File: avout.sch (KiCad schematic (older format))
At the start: 47 parts, among them CN6 AUDIO_VIDEO, M1 Modulator, Q3 2SC1815, Q81 BC547, Q82 BC547

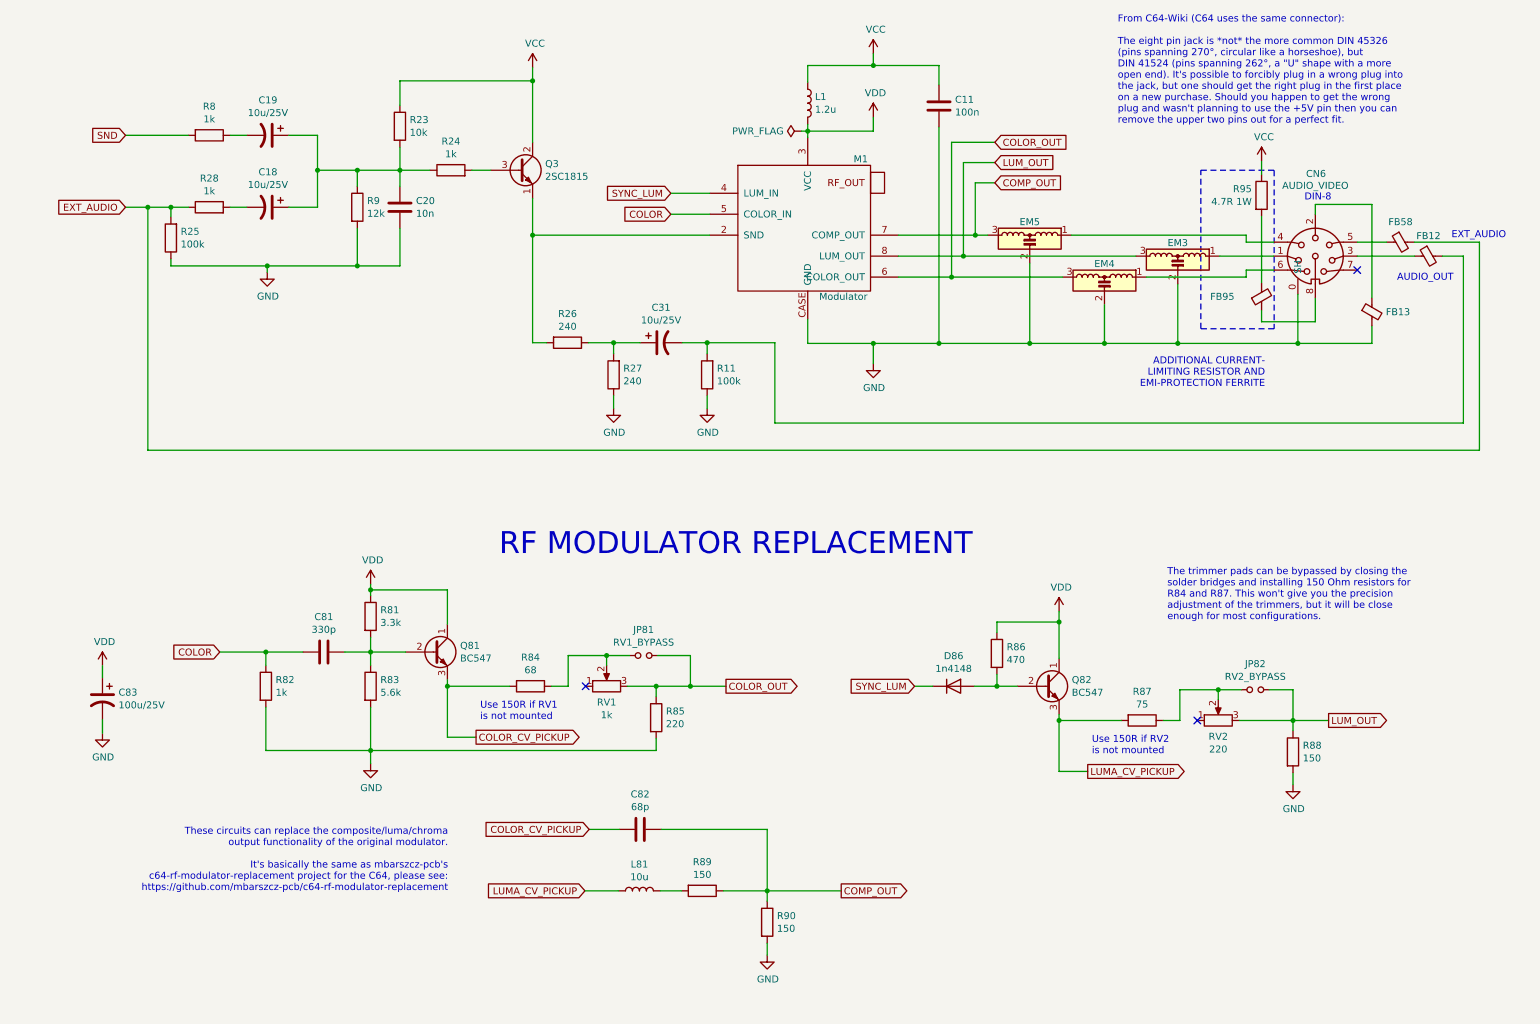
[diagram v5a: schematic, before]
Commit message: Isolate video ground
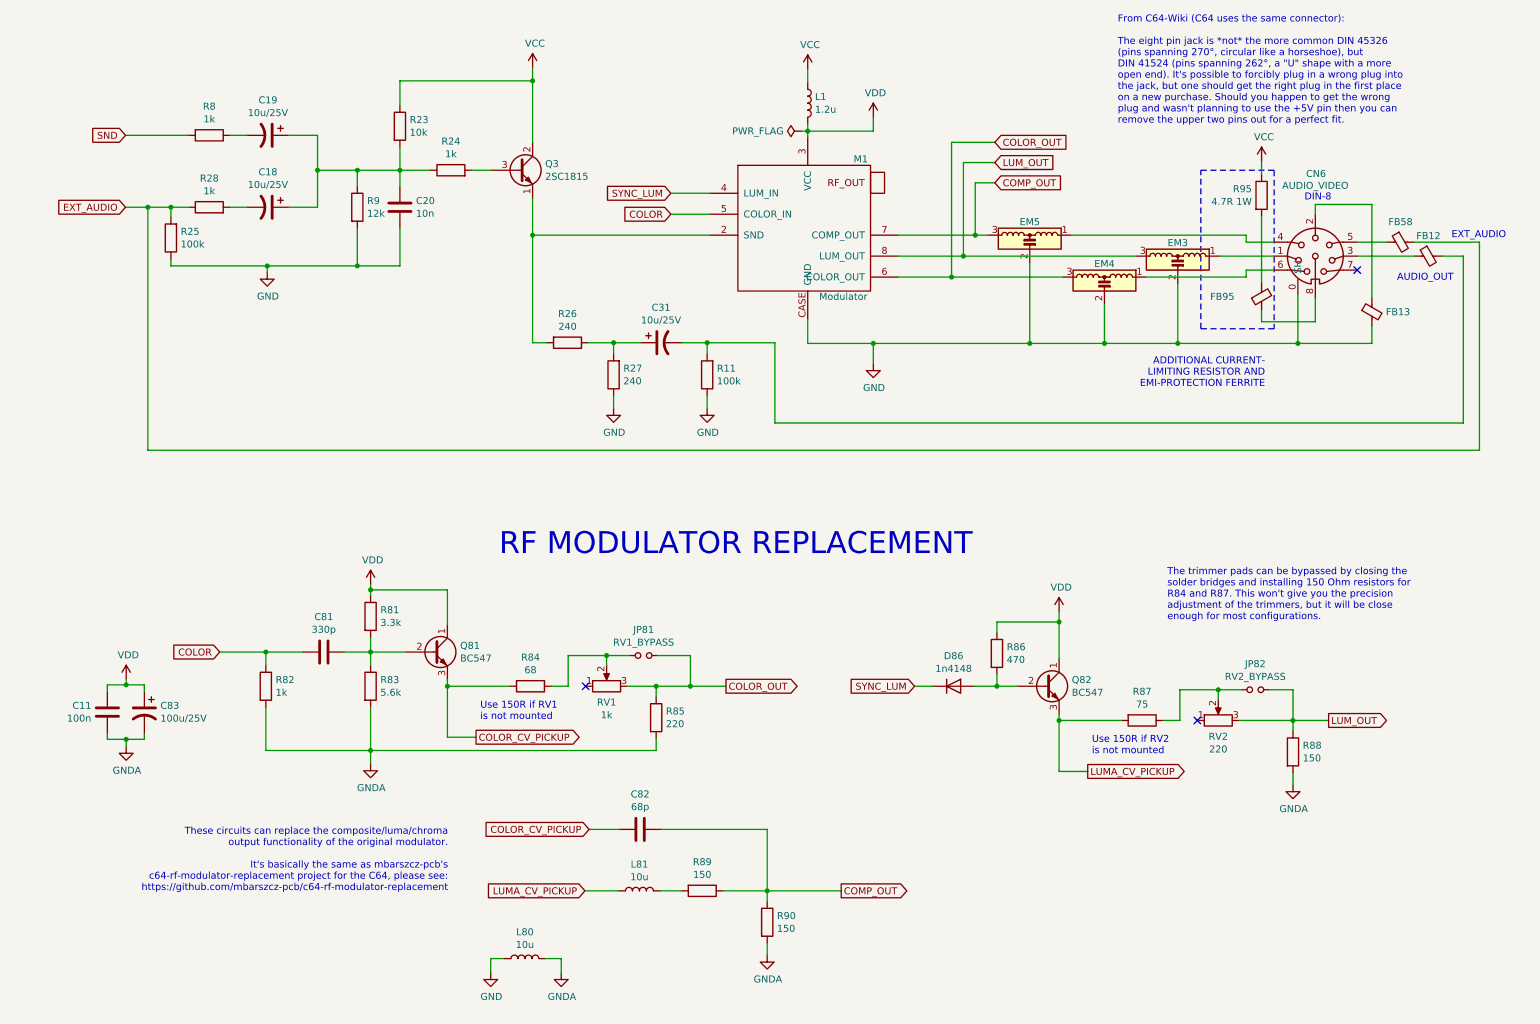
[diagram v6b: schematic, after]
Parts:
- added L80: 10u, Inductor_THT:L_Axial_L7.0mm_D3.3mm_P12.70mm_Horizontal_Fastron_MICC, symbol Device:L
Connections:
- net GND: now also L80.1; no longer C11.2, C83.2, R82.2, R83.2, R85.2, R88.2, R90.2
- net VCC: no longer C11.1
- net VDD: now also C11.1
- new net GNDA: C11.2, C83.2, L80.2, R82.2, R83.2, R85.2, R88.2, R90.2
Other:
- moved on the sheet: C11, C83
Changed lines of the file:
@@
 Sheet 12 12
 Title "LittleSixteen"
-Date "2021-11-29"
-Rev "3git"
+Date "2022-01-14"
+Rev "4git"
 Comp "SukkoPera"
 Comment1 "Licensed under CC BY-NC-SA 4.0"
@@
 L Device:C C11
 U 1 1 5E01CA58
-P 6950 1240
-F 0 "C11" H 7065 1286 50  0000 L CNN
-F 1 "100n" H 7065 1195 50  0000 L CNN
-F 2 "Capacitor_THT:C_Disc_D8.0mm_W2.5mm_P5.00mm" H 6988 1090 50  0001 C CNN
-F 3 "~" H 6950 1240 50  0001 C CNN
-	1    6950 1240
-	1    0    0    -1
-$EndComp
-Wire Wire Line
-	6950 1390 6950 2940
-Wire Wire Line
-	6950 2940 6480 2940
+P 995 5580
+F 0 "C11" H 880 5626 50  0000 R CNN
+F 1 "100n" H 880 5535 50  0000 R CNN
+F 2 "Capacitor_THT:C_Disc_D8.0mm_W2.5mm_P5.00mm" H 1033 5430 50  0001 C CNN
+F 3 "~" H 995 5580 50  0001 C CNN
+	1    995  5580
+	1    0    0    -1
+$EndComp
 Wire Wire Line
 	6010 2940 6010 2765
-$Comp
-L power:GND #PWR0177
-U 1 1 5E01E136
-P 6480 3085
-F 0 "#PWR0177" H 6480 2835 50  0001 C CNN
-F 1 "GND" H 6485 2912 50  0000 C CNN
-F 2 "" H 6480 3085 50  0001 C CNN
-F 3 "" H 6480 3085 50  0001 C CNN
-	1    6480 3085
-	1    0    0    -1
-$EndComp
 Wire Wire Line
 	6480 3085 6480 2940
@@
 	1    0    0    -1
 $EndComp
-$Comp
-L power:VCC #PWR0178
-U 1 1 5E021287
-P 6480 865
-F 0 "#PWR0178" H 6480 715 50  0001 C CNN
-F 1 "VCC" H 6497 1038 50  0000 C CNN
-F 2 "" H 6480 865 50  0001 C CNN
-F 3 "" H 6480 865 50  0001 C CNN
-	1    6480 865
-	1    0    0    -1
-$EndComp
-Wire Wire Line
-	6480 865  6480 950
 $Comp
 L Device:EMI_Filter_LCL EM5
@@
 	7600 2365 7600 2940
 Wire Wire Line
-	7600 2940 6950 2940
-Connection ~ 6950 2940
-Wire Wire Line
 	8135 2665 8135 2940
 Wire Wire Line
@@
 Wire Wire Line
 	4620 2935 4620 3015
-$Comp
-L power:GND #PWR0182
-U 1 1 5E0D9522
-P 4620 3405
-F 0 "#PWR0182" H 4620 3155 50  0001 C CNN
-F 1 "GND" H 4625 3232 50  0000 C CNN
-F 2 "" H 4620 3405 50  0001 C CNN
-F 3 "" H 4620 3405 50  0001 C CNN
-	1    4620 3405
-	1    0    0    -1
-$EndComp
 Wire Wire Line
 	4620 3405 4620 3315
@@
 Wire Wire Line
 	5290 2935 5290 3015
-$Comp
-L power:GND #PWR0183
-U 1 1 5E0E032C
-P 5290 3405
-F 0 "#PWR0183" H 5290 3155 50  0001 C CNN
-F 1 "GND" H 5295 3232 50  0000 C CNN
-F 2 "" H 5290 3405 50  0001 C CNN
-F 3 "" H 5290 3405 50  0001 C CNN
-	1    5290 3405
-	1    0    0    -1
-$EndComp
 Wire Wire Line
 	5290 3405 5290 3315
@@
 Text Notes 8230 1375 0    50   ~ 0
 From C64-Wiki (C64 uses the same connector):\n\nThe eight pin jack is *not* the more common DIN 45326\n(pins spanning 270°, circular like a horseshoe), but\nDIN 41524 (pins spanning 262°, a "U" shape with a more\nopen end). It's possible to forcibly plug in a wrong plug into\nthe jack, but one should get the right plug in the first place\non a new purchase. Should you happen to get the wrong\nplug and wasn't planning to use the +5V pin then you can\nremove the upper two pins out for a perfect fit.
-Wire Wire Line
-	6480 950  6950 950
-Connection ~ 6480 950
-Wire Wire Line
-	6950 950  6950 1090
-Wire Wire Line
-	6480 950  6010 950
-Wire Wire Line
-	6010 950  6010 1070
 Wire Wire Line
 	6010 1370 6010 1420
@@
 Wire Wire Line
 	2880 5855 2880 5950
-$Comp
-L power:GND #PWR083
-U 1 1 61A1F11D
-P 2880 5950
-F 0 "#PWR083" H 2880 5700 50  0001 C CNN
-F 1 "GND" H 2885 5777 50  0000 C CNN
-F 2 "" H 2880 5950 50  0001 C CNN
-F 3 "" H 2880 5950 50  0001 C CNN
-	1    2880 5950
-	1    0    0    -1
-$EndComp
 Wire Wire Line
 	2695 5150 2880 5150
@@
 Wire Wire Line
 	6905 5395 6775 5395
-$Comp
-L power:GND #PWR084
-U 1 1 61AA2886
-P 9485 6100
-F 0 "#PWR084" H 9485 5850 50  0001 C CNN
-F 1 "GND" H 9490 5927 50  0000 C CNN
-F 2 "" H 9485 6100 50  0001 C CNN
-F 3 "" H 9485 6100 50  0001 C CNN
-	1    9485 6100
-	1    0    0    -1
-$EndComp
 Text GLabel 5425 5395 2    50   Output ~ 0
 COLOR_OUT
@@
 Wire Wire Line
 	5720 7320 5720 7235
-$Comp
-L power:GND #PWR085
-U 1 1 61B1B1F1
-P 5720 7320
-F 0 "#PWR085" H 5720 7070 50  0001 C CNN
-F 1 "GND" H 5725 7147 50  0000 C CNN
-F 2 "" H 5720 7320 50  0001 C CNN
-F 3 "" H 5720 7320 50  0001 C CNN
-	1    5720 7320
-	1    0    0    -1
-$EndComp
 Connection ~ 5720 6860
 Wire Wire Line
@@
 L Device:CP1 C83
 U 1 1 61BCB802
-P 960 5485
-F 0 "C83" H 845 5531 50  0000 R CNN
-F 1 "100u/25V" H 845 5440 50  0000 R CNN
-F 2 "Capacitor_THT:CP_Radial_D6.3mm_P2.50mm" H 960 5485 50  0001 C CNN
-F 3 "~" H 960 5485 50  0001 C CNN
-	1    960  5485
+P 1260 5580
+F 0 "C83" H 1145 5626 50  0000 R CNN
+F 1 "100u/25V" H 1145 5535 50  0000 R CNN
+F 2 "Capacitor_THT:CP_Radial_D6.3mm_P2.50mm" H 1260 5580 50  0001 C CNN
+F 3 "~" H 1260 5580 50  0001 C CNN
+	1    1260 5580
 	-1   0    0    -1
 $EndComp
 Wire Wire Line
-	960  5250 960  5335
-Wire Wire Line
-	960  5635 960  5730
-$Comp
-L power:GND #PWR087
-U 1 1 61BD4A62
-P 960 5730
-F 0 "#PWR087" H 960 5480 50  0001 C CNN
-F 1 "GND" H 965 5557 50  0000 C CNN
-F 2 "" H 960 5730 50  0001 C CNN
-F 3 "" H 960 5730 50  0001 C CNN
-	1    960  5730
-	1    0    0    -1
-$EndComp
+	1130 5345 1130 5385
+Wire Wire Line
+	1260 5730 1260 5775
 Wire Wire Line
 	7040 2465 7040 1500
@@
 L power:VDD #PWR0200
 U 1 1 61C8FCEC
-P 960 5250
-F 0 "#PWR0200" H 960 5100 50  0001 C CNN
-F 1 "VDD" H 975 5423 50  0000 C CNN
-F 2 "" H 960 5250 50  0001 C CNN
-F 3 "" H 960 5250 50  0001 C CNN
-	1    960  5250
+P 1130 5345
+F 0 "#PWR0200" H 1130 5195 50  0001 C CNN
+F 1 "VDD" H 1145 5518 50  0000 C CNN
+F 2 "" H 1130 5345 50  0001 C CNN
+F 3 "" H 1130 5345 50  0001 C CNN
+	1    1130 5345
 	1    0    0    -1
 $EndComp
@@
 Text Notes 9285 3260 2    50   ~ 0
 ADDITIONAL CURRENT-\nLIMITING RESISTOR AND\nEMI-PROTECTION FERRITE
+$Comp
+L power:GNDA #PWR0232
+U 1 1 61E6D037
+P 2880 5950
+F 0 "#PWR0232" H 2880 5700 50  0001 C CNN
+F 1 "GNDA" H 2885 5777 50  0000 C CNN
+F 2 "" H 2880 5950 50  0001 C CNN
+F 3 "" H 2880 5950 50  0001 C CNN
+	1    2880 5950
+	1    0    0    -1
+$EndComp
+$Comp
+L power:GNDA #PWR0233
+U 1 1 61E7DA1B
+P 1130 5825
+F 0 "#PWR0233" H 1130 5575 50  0001 C CNN
+F 1 "GNDA" H 1135 5652 50  0000 C CNN
+F 2 "" H 1130 5825 50  0001 C CNN
+F 3 "" H 1130 5825 50  0001 C CNN
+	1    1130 5825
+	1    0    0    -1
+$EndComp
+$Comp
+L power:GNDA #PWR0234
+U 1 1 61E85F57
+P 5720 7320
+F 0 "#PWR0234" H 5720 7070 50  0001 C CNN
+F 1 "GNDA" H 5725 7147 50  0000 C CNN
+F 2 "" H 5720 7320 50  0001 C CNN
+F 3 "" H 5720 7320 50  0001 C CNN
+	1    5720 7320
+	1    0    0    -1
+$EndComp
+$Comp
+L power:GNDA #PWR0235
+U 1 1 61E86672
+P 9485 6100
+F 0 "#PWR0235" H 9485 5850 50  0001 C CNN
+F 1 "GNDA" H 9490 5927 50  0000 C CNN
+F 2 "" H 9485 6100 50  0001 C CNN
+F 3 "" H 9485 6100 50  0001 C CNN
+	1    9485 6100
+	1    0    0    -1
+$EndComp
+$Comp
+L power:GNDA #PWR0236
+U 1 1 61E8FEF8
+P 4245 7445
+F 0 "#PWR0236" H 4245 7195 50  0001 C CNN
+F 1 "GNDA" H 4250 7272 50  0000 C CNN
+F 2 "" H 4245 7445 50  0001 C CNN
+F 3 "" H 4245 7445 50  0001 C CNN
+	1    4245 7445
+	1    0    0    -1
+$EndComp
+$Comp
+L power:GND #PWR0237
+U 1 1 61E90996
+P 3740 7445
+F 0 "#PWR0237" H 3740 7195 50  0001 C CNN
+F 1 "GND" H 3745 7272 50  0000 C CNN
+F 2 "" H 3740 7445 50  0001 C CNN
+F 3 "" H 3740 7445 50  0001 C CNN
+	1    3740 7445
+	1    0    0    -1
+$EndComp
+Wire Wire Line
+	3740 7445 3740 7345
+Wire Wire Line
+	3740 7345 3835 7345
+$Comp
+L Device:L L80
+U 1 1 61E8F0DE
+P 3985 7345
+F 0 "L80" V 4175 7345 50  0000 C CNN
+F 1 "10u" V 4084 7345 50  0000 C CNN
+F 2 "Inductor_THT:L_Axial_L7.0mm_D3.3mm_P12.70mm_Horizontal_Fastron_MICC" H 3985 7345 50  0001 C CNN
+F 3 "~" H 3985 7345 50  0001 C CNN
+	1    3985 7345
+	0    -1   -1   0
+$EndComp
+Wire Wire Line
+	4135 7345 4245 7345
+Wire Wire Line
+	4245 7345 4245 7445
+$Comp
+L power:GND #PWR0183
+U 1 1 5E0E032C
+P 5290 3405
+F 0 "#PWR0183" H 5290 3155 50  0001 C CNN
+F 1 "GND" H 5295 3232 50  0000 C CNN
+F 2 "" H 5290 3405 50  0001 C CNN
+F 3 "" H 5290 3405 50  0001 C CNN
+	1    5290 3405
+	1    0    0    -1
+$EndComp
+$Comp
+L power:GND #PWR0182
+U 1 1 5E0D9522
+P 4620 3405
+F 0 "#PWR0182" H 4620 3155 50  0001 C CNN
+F 1 "GND" H 4625 3232 50  0000 C CNN
+F 2 "" H 4620 3405 50  0001 C CNN
+F 3 "" H 4620 3405 50  0001 C CNN
+	1    4620 3405
+	1    0    0    -1
+$EndComp
+$Comp
+L power:GND #PWR0177
+U 1 1 5E01E136
+P 6480 3085
+F 0 "#PWR0177" H 6480 2835 50  0001 C CNN
+F 1 "GND" H 6485 2912 50  0000 C CNN
+F 2 "" H 6480 3085 50  0001 C CNN
+F 3 "" H 6480 3085 50  0001 C CNN
+	1    6480 3085
+	1    0    0    -1
+$EndComp
+Wire Wire Line
+	995  5430 995  5385
+Wire Wire Line
+	995  5385 1130 5385
+Wire Wire Line
+	1260 5385 1260 5430
+Connection ~ 1130 5385
+Wire Wire Line
+	1130 5385 1260 5385
+Wire Wire Line
+	995  5730 995  5775
+Wire Wire Line
+	995  5775 1130 5775
+Wire Wire Line
+	1130 5775 1130 5825
+Connection ~ 1130 5775
+Wire Wire Line
+	1130 5775 1260 5775
+Wire Wire Line
+	6480 2940 7600 2940
+$Comp
+L power:VCC #PWR0178
+U 1 1 5E021287
+P 6010 975
+F 0 "#PWR0178" H 6010 825 50  0001 C CNN
+F 1 "VCC" H 6027 1148 50  0000 C CNN
+F 2 "" H 6010 975 50  0001 C CNN
+F 3 "" H 6010 975 50  0001 C CNN
+	1    6010 975
+	1    0    0    -1
+$EndComp
+Wire Wire Line
+	6010 975  6010 1070
 $EndSCHEMATC

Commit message: Improve video output - Thanks @kinmami!
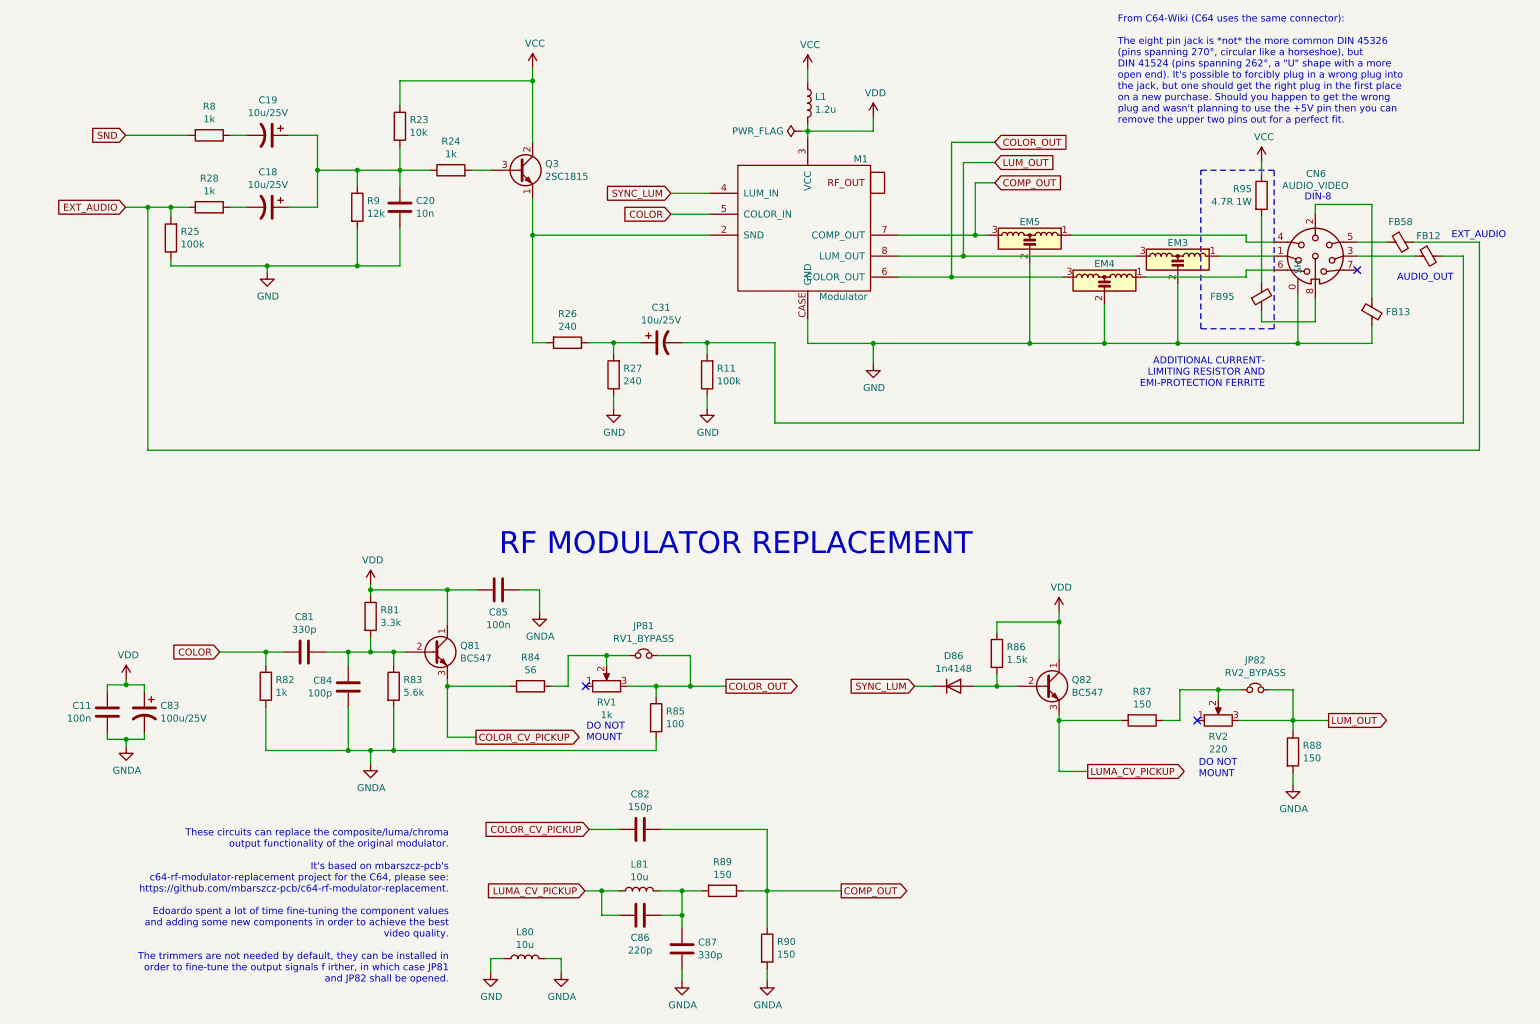
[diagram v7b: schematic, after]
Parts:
- removed JP81: RV1_BYPASS, Jumper:SolderJumper-2_P1.3mm_Open_RoundedPad1.0x1.5mm, symbol Device:Jumper_NO_Small
- removed JP82: RV2_BYPASS, Jumper:SolderJumper-2_P1.3mm_Open_RoundedPad1.0x1.5mm, symbol Device:Jumper_NO_Small
- added C84: 100p, Capacitor_THT:C_Disc_D8.0mm_W2.5mm_P5.00mm, symbol Device:C
- added C85: 100n, Capacitor_THT:C_Disc_D8.0mm_W2.5mm_P5.00mm, symbol Device:C
- added C86: 220p, Capacitor_THT:C_Disc_D8.0mm_W2.5mm_P5.00mm, symbol Device:C
- added C87: 330p, Capacitor_THT:C_Disc_D8.0mm_W2.5mm_P5.00mm, symbol Device:C
- added JP81: RV1_BYPASS, Jumper:SolderJumper-2_P1.3mm_Bridged_RoundedPad1.0x1.5mm, symbol Device:Jumper_NC_Small
- added JP82: RV2_BYPASS, Jumper:SolderJumper-2_P1.3mm_Bridged_RoundedPad1.0x1.5mm, symbol Device:Jumper_NC_Small
- C82: value 68p -> 150p
- R84: value 68 -> 56
- R85: value 220 -> 100
- R86: value 470 -> 1.5k
- R87: value 75 -> 150
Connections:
- net COLOR_OUT: now also JP81.2
- net GNDA: now also C84.1, C85.2, C87.1
- net LUMA_CV_PICKUP: now also C86.2
- net LUM_OUT: now also JP82.2
- net VDD: now also C85.1
- net at C81.1, Q81.2 (B), R81.2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: now also C84.2
- net at R84.1, RV1.2: now also JP81.1
- net at R87.1, RV2.2: now also JP82.1
- net at L81.2, R89.2: now also C86.1, C87.2
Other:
- note added: "DO NOT\nMOUNT"
- note added: "These circuits can replace the composite/luma/chroma\noutput functionality of the original modulator.\n\nIt's based on mbarszcz-pcb's\nc64-rf-modulator-replacement project for the C64, please see:\nhttps://github.com/mbarszcz-pcb/c64-rf-modulator-replacement.\n\nEdoardo spent a lot of time fine-tuning the component values\nand adding some new components in order to achieve the best\nvideo quality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"
- note removed: "The trimmer pads can be bypassed by closing the\nsolder bridges and installing 150 Ohm resistors for\nR84 and R87. This won't give you the precision\nadjustment of the trimmers, but it will be close\nenough for most configurations."
- note removed: "These circuits can replace the composite/luma/chroma\noutput functionality of the original modulator.\n\nIt's basically the same as mbarszcz-pcb's\nc64-rf-modulator-replacement project for the C64, please see:\nhttps://github.com/mbarszcz-pcb/c64-rf-modulator-replacement"
- note removed: "Use 150R if RV1\nis not mounted"
- note removed: "Use 150R if RV2\nis not mounted"
- moved on the sheet: C81, R83, R89, R90
